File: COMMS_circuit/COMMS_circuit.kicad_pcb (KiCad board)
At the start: 4 copper layers, 40.6 x 115.5 mm, 212 parts, among them J1 SMA, J2 SMA, J3 USB_C_Receptacle_USB2.0_14P, J4 Conn_01x02_Pin, U1 max19713etn+, U10 FT2232HL, U11 93LC56, U12 ADP7105ACPZ-R7, U13 ADP7105ACPZ-R7, U14 TPS2121RUXR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

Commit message: Changes I missed cause id been staring at it to long
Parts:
- moved C95 2.80 mm to (114.8, 100.5)
- moved C6 0.35 mm to (94.9, 64.0)
- moved C42 0.20 mm to (93.8, 63.3)
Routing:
- net +3V3: track 101.5 -> 116.5 mm, vias 29 -> 33
- net AGND: track 80.0 -> 87.3 mm, vias 32 -> 34
- net DGND: track 73.1 -> 75.1 mm, vias 24 -> 27
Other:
- board size 40.6 x 115.5 mm -> 40.6 x 116 mm

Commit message: testing opsec update
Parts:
- added J5: Conn_01x12_Pin, Connector_PinHeader_2.54mm:PinHeader_1x12_P2.54mm_Vertical, F.Cu at (79.5, 77.3)
- added R58: 1k, Resistor_SMD:R_0402_1005Metric, F.Cu at (105.3, 51.0)
- added R59: 1k, Resistor_SMD:R_0402_1005Metric, F.Cu at (106.4, 51.0)
- added R60: 1k, Resistor_SMD:R_0402_1005Metric, F.Cu at (96.5, 48.8)
- added R61: 1k, Resistor_SMD:R_0402_1005Metric, F.Cu at (98.2, 49.0)
- added REF**: BalloonArt, BPP_Lib:BalloonArt, F.Cu at (86.2, 130.2)
- L16, L17, L18, L19: value 12u -> 360n
- moved C59 2.75 mm to (87.8, 86.0), turned to -90 degrees
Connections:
- U15 pad 1: unconnected-(U15D-IOL_2A-Pad1) -> /TTCK
- U15 pad 10: unconnected-(U15D-IOL_5B-Pad10) -> Net-(J5-Pin_5)
- U15 pad 11: unconnected-(U15D-IOL_8A-Pad11) -> Net-(J5-Pin_6)
- U15 pad 12: unconnected-(U15D-IOL_8B-Pad12) -> Net-(J5-Pin_7)
- U15 pad 15: unconnected-(U15D-IOL_10A-Pad15) -> Net-(J5-Pin_8)
- U15 pad 16: unconnected-(U15D-IOL_10B-Pad16) -> Net-(J5-Pin_9)
- U15 pad 17: unconnected-(U15D-IOL_12A-Pad17) -> Net-(J5-Pin_10)
- U15 pad 7: unconnected-(U15D-IOL_4A-Pad7) -> Net-(J5-Pin_2)
- U15 pad 8: unconnected-(U15D-IOL_4B-Pad8) -> Net-(J5-Pin_3)
- U15 pad 9: unconnected-(U15D-IOL_5A-Pad9) -> Net-(J5-Pin_4)
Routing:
- net /TTCK: track 0.00 -> 61.5 mm, vias 0 -> 2
- net +5V: track 121.3 -> 156.0 mm
- net DGND: track 75.1 -> 97.5 mm, vias 27 -> 180
- net Net-(J5-Pin_2): track 0.00 -> 13.4 mm
- net Net-(J5-Pin_10): track 0.00 -> 13.2 mm
- net Net-(J5-Pin_3): track 0.00 -> 12.5 mm
- net AGND: track 87.3 -> 99.8 mm, vias 34 -> 146
- net Net-(J5-Pin_9): track 0.00 -> 12.3 mm
- net Net-(J5-Pin_4): track 0.00 -> 11.7 mm
- net Net-(J5-Pin_8): track 0.00 -> 11.5 mm
- net Net-(J3-VBUS-PadA4): track 2.78 -> 14.1 mm
- net Net-(J5-Pin_7): track 0.00 -> 11.1 mm
- net Net-(J5-Pin_5): track 0.00 -> 10.8 mm
- net Net-(J5-Pin_6): track 0.00 -> 10.2 mm
- net +3V3: track 116.5 -> 124.3 mm, vias 33 -> 35
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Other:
- outline, holes or cut-outs redrawn
- board text added: "UMD BPP COMMS Phase 1 V1 Herman Moeller 2-6-25"

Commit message: fix all noticed problems
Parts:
- moved X2 1.31 mm to (87.8, 104.7), turned to 90 degrees
- moved X1 0.35 mm to (86.8, 82.8), turned to 180 degrees
- moved X3 0.21 mm to (89.5, 124.5), turned to -90 degrees
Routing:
- net +3V3: track 124.3 -> 130.1 mm, vias 35 -> 36
- net DGND: track 97.5 -> 95.7 mm, vias 180 -> 179
- net +1V2: track 101.6 -> 99.9 mm
- net /SYS_clk: track 12.7 -> 11.4 mm
- net /Power/VIN: track 114.8 -> 114.1 mm

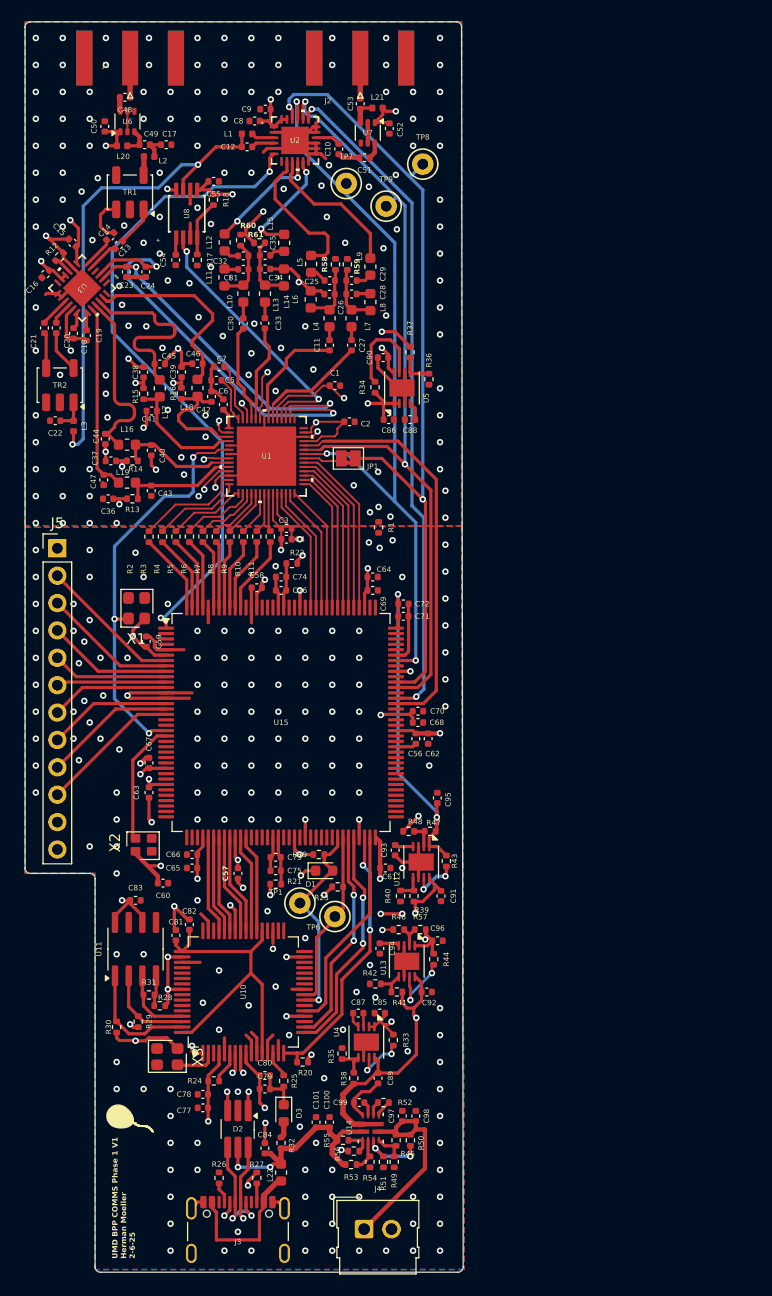
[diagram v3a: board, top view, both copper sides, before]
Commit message: Stick a RP2040 on the side and see if we can program an FPGA with it
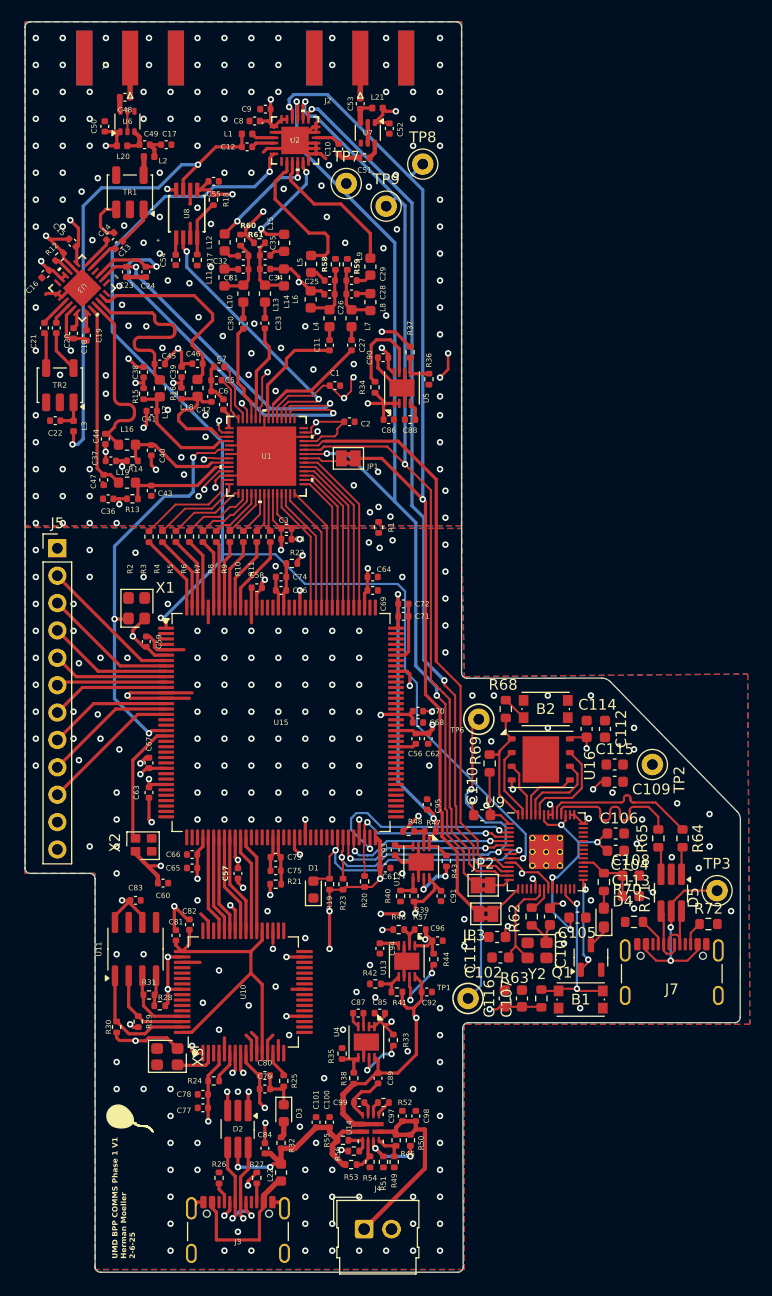
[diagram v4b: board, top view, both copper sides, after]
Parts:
- added B1: KMR2, Button_Switch_SMD:SW_Push_1P1T_NO_CK_KMR2, F.Cu at (128.1, 119.2)
- added B2: KMR2, Button_Switch_SMD:SW_Push_1P1T_NO_CK_KMR2, F.Cu at (124.8, 92.2)
- added C102: 10pF, Capacitor_SMD:C_0603_1608Metric, F.Cu at (120.6, 115.3)
- added C103: 10pF, Capacitor_SMD:C_0603_1608Metric, F.Cu at (125.2, 111.5)
- added C104: 100nF, Capacitor_SMD:C_0603_1608Metric, F.Cu at (131.3, 105.4)
- added C105: 100nF, Capacitor_SMD:C_0603_1608Metric, F.Cu at (127.8, 111.6)
- added C106: 1uF, Capacitor_SMD:C_0603_1608Metric, F.Cu at (131.3, 103.8)
- added C107: 1uF, Capacitor_SMD:C_0603_1608Metric, F.Cu at (122.6, 119.1)
- added C108: 100nF, Capacitor_SMD:C_0603_1608Metric, F.Cu at (132.7, 107.7)
- added C109: 100nF, Capacitor_SMD:C_0603_1608Metric, F.Cu at (131.2, 99.0)
- added C110: 100nF, Capacitor_SMD:C_0603_1608Metric, F.Cu at (118.9, 102.1)
- added C111: 100nF, Capacitor_SMD:C_0603_1608Metric, F.Cu at (120.3, 113.4)
- added C112: 10uF, Capacitor_SMD:C_0603_1608Metric, F.Cu at (130.3, 94.1)
- added C113: 100nF, Capacitor_SMD:C_0603_1608Metric, F.Cu at (132.7, 109.6)
- added C114: 100nF, Capacitor_SMD:C_0603_1608Metric, F.Cu at (128.6, 94.1)
- added C115: 100nF, Capacitor_SMD:C_0603_1608Metric, F.Cu at (131.2, 97.4)
- added C116: 100nF, Capacitor_SMD:C_0603_1608Metric, F.Cu at (121.0, 119.1)
- added D4: LED, Diode_SMD:D_0603_1608Metric_Pad1.05x0.95mm_HandSolder, F.Cu at (130.2, 111.6)
- added D5: USBLC6-2SC6, Package_TO_SOT_SMD:TSOT-23-6_HandSoldering, F.Cu at (136.4, 109.3)
- added J7: USB_C_Receptacle_USB2.0, Connector_USB:USB_C_Receptacle_GCT_USB4105-xx-A_16P_TopMnt_Horizontal, F.Cu at (136.5, 117.8)
- added JP2: Jumper_2_Bridged, Jumper:SolderJumper-2_P1.3mm_Bridged2Bar_Pad1.0x1.5mm, F.Cu at (119.0, 108.6)
- added JP3: Jumper_2_Bridged, Jumper:SolderJumper-2_P1.3mm_Bridged2Bar_Pad1.0x1.5mm, F.Cu at (119.2, 111.2)
- added Q1: IRLML0060TRPBF, Package_TO_SOT_SMD:SOT-23-3, F.Cu at (129.0, 115.3)
- added R62: 1k, Resistor_SMD:R_0603_1608Metric, F.Cu at (123.5, 111.5)
- added R63: 10k, Resistor_SMD:R_0603_1608Metric, F.Cu at (124.4, 119.1)
- added R64: 27, Resistor_SMD:R_0603_1608Metric, F.Cu at (137.5, 104.2)
- added R65: 27, Resistor_SMD:R_0603_1608Metric, F.Cu at (135.2, 104.2)
- added R68: 1k, Resistor_SMD:R_0603_1608Metric, F.Cu at (121.1, 92.2)
- added R69: 10k, Resistor_SMD:R_0603_1608Metric, F.Cu at (119.6, 97.3)
- added R70: 590, Resistor_SMD:R_0603_1608Metric, F.Cu at (130.2, 108.3)
- added R71: 5.1k, Resistor_SMD:R_0603_1608Metric, F.Cu at (133.0, 112.0)
- added R72: 5.1k, Resistor_SMD:R_0603_1608Metric, F.Cu at (139.9, 112.2)
- added TP2: TestPoint, TestPoint:TestPoint_Keystone_5000-5004_Miniature, F.Cu at (134.7, 97.4)
- added TP3: TestPoint, TestPoint:TestPoint_Keystone_5000-5004_Miniature, F.Cu at (140.7, 109.1)
- added U16: W25Q64JVZP, Package_SON:WSON-8-1EP_6x5mm_P1.27mm_EP3.4x4.3mm, F.Cu at (124.3, 96.9)
- added U9: RP2040, BPP_Lib:RP2040-QFN-56, F.Cu at (124.8, 105.5)
- added Y2: 12MHz, Crystal:Crystal_SMD_2520-4Pin_2.5x2.0mm, F.Cu at (124.0, 114.6)
- moved TP6 22.7 mm to (118.6, 93.2)
- moved TP1 17.9 mm to (117.6, 119.1)
- moved R20 17.7 mm to (108.0, 108.2), turned to 90 degrees
- moved R19 2.93 mm to (104.8, 108.5), turned to 90 degrees
- moved D1 2.02 mm to (103.2, 109.0), turned to 90 degrees
- moved C95 1.12 mm to (113.8, 101.1)
- moved R23 0.56 mm to (106.0, 108.5), turned to 90 degrees
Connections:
- U10 pad 16: /HOST_SCK -> /USB/Ice_SCK
- U10 pad 17: /HOST_MOSI -> /USB/FLASH_MOSI
- U10 pad 18: /HOST_MISO -> /USB/FLASH_MISO
- U10 pad 21: /HOST_SS -> /USB/iCE_SS_B
- U10 pad 23: /ICE_CDONE -> /USB/iCE_CDONE
- U10 pad 24: /ICE_CRESET -> /USB/iCE_CREST
- U15 pad 102: /SPI_SDI -> /ICE40HX8k-CB132/SPI_SDI
- U15 pad 94: /SPI_CS_FE -> /ICE40HX8k-CB132/SPI_CS_FE
- U15 pad 95: /SPI_CS_M -> /ICE40HX8k-CB132/SPI_CS_M
- U15 pad 97: /SPI_CLK -> /ICE40HX8k-CB132/SPI_CLK
- U15 pad 98: /SPI_SDO -> /ICE40HX8k-CB132/SPI_SDO
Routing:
- net /TTCK: track 61.5 -> 110.7 mm, vias 2 -> 3
- net +3V3: track 130.1 -> 175.1 mm, vias 36 -> 47
- net Net-(U9-VREG_VOUT): track 0.00 -> 22.2 mm, vias 0 -> 4
- net /SPI_SDO: track 75.7 -> 97.2 mm
- net /SPI_SDI: track 71.0 -> 92.3 mm
- net /ICE_CDONE: track 19.5 -> 39.6 mm, vias 1 -> 2
- net /SPI_CLK: track 75.4 -> 94.8 mm
- net /ICE_CRESET: track 16.6 -> 36.1 mm, vias 0 -> 3
- net /SPI_CS_M: track 62.5 -> 81.1 mm
- net Net-(D5-VP): track 0.00 -> 16.8 mm, vias 0 -> 2
- net /SPI_CS_FE: track 37.8 -> 53.7 mm
- net Net-(U9-RUN): track 0.00 -> 15.8 mm, vias 0 -> 2
- net Net-(U9-USB_DM): track 0.00 -> 14.9 mm
- net Net-(U9-USB_DP): track 0.00 -> 14.5 mm
- net /QSPI_SS: track 0.00 -> 11.4 mm
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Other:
- board size 40.6 x 116 mm -> 66.4 x 116 mm
